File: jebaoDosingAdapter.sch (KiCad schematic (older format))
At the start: 4 parts, among them J1 Conn_01x05_Male, J2 Conn_01x02_Male, J3 6P6C, U1 ULN2803A

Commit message: Add images and updated gerbers
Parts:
- added H1, H2, H3, H4: MountingHole, MountingHole:MountingHole_3.2mm_M3, symbol Mechanical:MountingHole
- J1: footprint Connector_PinHeader_2.54mm:PinHeader_1x05_P2.54mm_Vertical -> Connector_JST:JST_XH_B05B-XH-A_1x05_P2.50mm_Vertical
- J2: footprint Connector_PinHeader_2.54mm:PinHeader_1x02_P2.54mm_Vertical -> Connector_JST:JST_XH_B02B-XH-A_1x02_P2.50mm_Vertical
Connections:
- net O1: now reaches J3.4
- net O1: now also U1.18 (O1); no longer U1.15 (O4)
- net O2: now reaches J3.2
- net O2: now also U1.17 (O2); no longer U1.16 (O3)
- net O3: now reaches J3.3
- net O3: now also U1.16 (O3); no longer U1.17 (O2)
- net O4: now reaches J3.5
- net O4: now also U1.15 (O4); no longer U1.18 (O1)
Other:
- moved on the sheet: J3
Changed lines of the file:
@@
 EESchema Schematic File Version 4
 LIBS:jebaoDosingAdapter-cache
-EELAYER 29 0
+EELAYER 26 0
 EELAYER END
 $Descr A4 11693 8268
@@
 $EndComp
 $Comp
-L Connector:6P6C J3
-U 1 1 5D71C0A6
-P 6600 2750
-F 0 "J3" H 6270 2754 50  0000 R CNN
-F 1 "6P6C" H 6270 2845 50  0000 R CNN
-F 2 "jebaoDosingAdapter:RJ11" V 6600 2775 50  0001 C CNN
-F 3 "~" V 6600 2775 50  0001 C CNN
-	1    6600 2750
-	-1   0    0    -1
-$EndComp
-$Comp
 L Connector:Conn_01x02_Male J2
 U 1 1 5D71C249
@@
 F 0 "J2" H 6706 3628 50  0000 C CNN
 F 1 "Conn_01x02_Male" H 6300 3400 50  0000 C CNN
-F 2 "Connector_PinHeader_2.54mm:PinHeader_1x02_P2.54mm_Vertical" H 6600 3450 50  0001 C CNN
+F 2 "Connector_JST:JST_XH_B02B-XH-A_1x02_P2.50mm_Vertical" H 6600 3450 50  0001 C CNN
 F 3 "~" H 6600 3450 50  0001 C CNN
 	1    6600 3450
@@
 F 0 "J1" H 4356 3128 50  0000 C CNN
 F 1 "Conn_01x05_Male" H 4356 3037 50  0000 C CNN
-F 2 "Connector_PinHeader_2.54mm:PinHeader_1x05_P2.54mm_Vertical" H 4250 2750 50  0001 C CNN
+F 2 "Connector_JST:JST_XH_B05B-XH-A_1x05_P2.50mm_Vertical" H 4250 2750 50  0001 C CNN
 F 3 "~" H 4250 2750 50  0001 C CNN
 	1    4250 2750
@@
 L power:+12V #PWR04
 U 1 1 5D71CEE9
-P 6150 3000
-F 0 "#PWR04" H 6150 2850 50  0001 C CNN
-F 1 "+12V" H 6165 3173 50  0000 C CNN
-F 2 "" H 6150 3000 50  0001 C CNN
-F 3 "" H 6150 3000 50  0001 C CNN
-	1    6150 3000
+P 6700 2850
+F 0 "#PWR04" H 6700 2700 50  0001 C CNN
+F 1 "+12V" H 6715 3023 50  0000 C CNN
+F 2 "" H 6700 2850 50  0001 C CNN
+F 3 "" H 6700 2850 50  0001 C CNN
+	1    6700 2850
 	1    0    0    1
 $EndComp
 Wire Wire Line
-	6150 3000 6150 2950
-Wire Wire Line
-	6150 2950 6200 2950
+	6700 2850 6700 2800
+Wire Wire Line
+	6700 2800 6750 2800
 $Comp
 L power:+12V #PWR05
 U 1 1 5D7302C7
-P 6150 2450
-F 0 "#PWR05" H 6150 2300 50  0001 C CNN
-F 1 "+12V" V 6165 2578 50  0000 L CNN
-F 2 "" H 6150 2450 50  0001 C CNN
-F 3 "" H 6150 2450 50  0001 C CNN
-	1    6150 2450
-	0    -1   1    0
-$EndComp
-Wire Wire Line
-	6200 2450 6150 2450
-Wire Wire Line
-	6200 2550 5700 2550
-Wire Wire Line
-	6200 2750 5950 2750
-Wire Wire Line
-	5950 2750 5950 2650
-Wire Wire Line
-	5950 2650 5700 2650
-Wire Wire Line
-	6200 2850 5900 2850
-Wire Wire Line
-	5900 2850 5900 2750
-Wire Wire Line
-	5900 2750 5700 2750
-Wire Wire Line
-	6200 2650 6050 2650
-Wire Wire Line
-	6050 2650 6050 2900
-Wire Wire Line
-	6050 2900 5850 2900
-Wire Wire Line
-	5850 2900 5850 2850
-Wire Wire Line
-	5850 2850 5700 2850
+P 6700 2300
+F 0 "#PWR05" H 6700 2150 50  0001 C CNN
+F 1 "+12V" H 6600 2450 50  0000 L CNN
+F 2 "" H 6700 2300 50  0001 C CNN
+F 3 "" H 6700 2300 50  0001 C CNN
+	1    6700 2300
+	-1   0    0    -1
+$EndComp
+Wire Wire Line
+	6750 2300 6700 2300
+$Comp
+L Mechanical:MountingHole H1
+U 1 1 5D9A0E71
+P 7850 2550
+F 0 "H1" H 7950 2596 50  0000 L CNN
+F 1 "MountingHole" H 7950 2505 50  0000 L CNN
+F 2 "MountingHole:MountingHole_3.2mm_M3" H 7850 2550 50  0001 C CNN
+F 3 "~" H 7850 2550 50  0001 C CNN
+	1    7850 2550
+	1    0    0    -1
+$EndComp
+$Comp
+L Mechanical:MountingHole H2
+U 1 1 5D9A0EAC
+P 7850 2750
+F 0 "H2" H 7950 2796 50  0000 L CNN
+F 1 "MountingHole" H 7950 2705 50  0000 L CNN
+F 2 "MountingHole:MountingHole_3.2mm_M3" H 7850 2750 50  0001 C CNN
+F 3 "~" H 7850 2750 50  0001 C CNN
+	1    7850 2750
+	1    0    0    -1
+$EndComp
+$Comp
+L Mechanical:MountingHole H3
+U 1 1 5D9A0ED0
+P 7850 2950
+F 0 "H3" H 7950 2996 50  0000 L CNN
+F 1 "MountingHole" H 7950 2905 50  0000 L CNN
+F 2 "MountingHole:MountingHole_3.2mm_M3" H 7850 2950 50  0001 C CNN
+F 3 "~" H 7850 2950 50  0001 C CNN
+	1    7850 2950
+	1    0    0    -1
+$EndComp
+$Comp
+L Mechanical:MountingHole H4
+U 1 1 5D9A0EFA
+P 7850 3150
+F 0 "H4" H 7950 3196 50  0000 L CNN
+F 1 "MountingHole" H 7950 3105 50  0000 L CNN
+F 2 "MountingHole:MountingHole_3.2mm_M3" H 7850 3150 50  0001 C CNN
+F 3 "~" H 7850 3150 50  0001 C CNN
+	1    7850 3150
+	1    0    0    -1
+$EndComp
+$Comp
+L Connector:6P6C J3
+U 1 1 5D71C0A6
+P 7150 2600
+F 0 "J3" H 6820 2604 50  0000 R CNN
+F 1 "6P6C" H 6820 2695 50  0000 R CNN
+F 2 "jebaoDosingAdapter:RJ11" V 7150 2625 50  0001 C CNN
+F 3 "~" V 7150 2625 50  0001 C CNN
+	1    7150 2600
+	-1   0    0    -1
+$EndComp
+Wire Wire Line
+	5700 2550 5900 2550
+Wire Wire Line
+	5700 2650 5900 2650
+Wire Wire Line
+	5700 2750 5900 2750
+Wire Wire Line
+	5700 2850 5900 2850
+Wire Wire Line
+	6750 2400 6450 2400
+Wire Wire Line
+	6750 2500 6450 2500
+Wire Wire Line
+	6750 2600 6450 2600
+Wire Wire Line
+	6750 2700 6450 2700
+Text Label 5900 2550 0    50   ~ 0
+O1
+Text Label 6450 2500 0    50   ~ 0
+O1
+Text Label 5900 2650 0    50   ~ 0
+O2
+Text Label 6450 2700 0    50   ~ 0
+O2
+Text Label 5900 2750 0    50   ~ 0
+O3
+Text Label 6450 2600 0    50   ~ 0
+O3
+Text Label 5900 2850 0    50   ~ 0
+O4
+Text Label 6450 2400 0    50   ~ 0
+O4
 $EndSCHEMATC

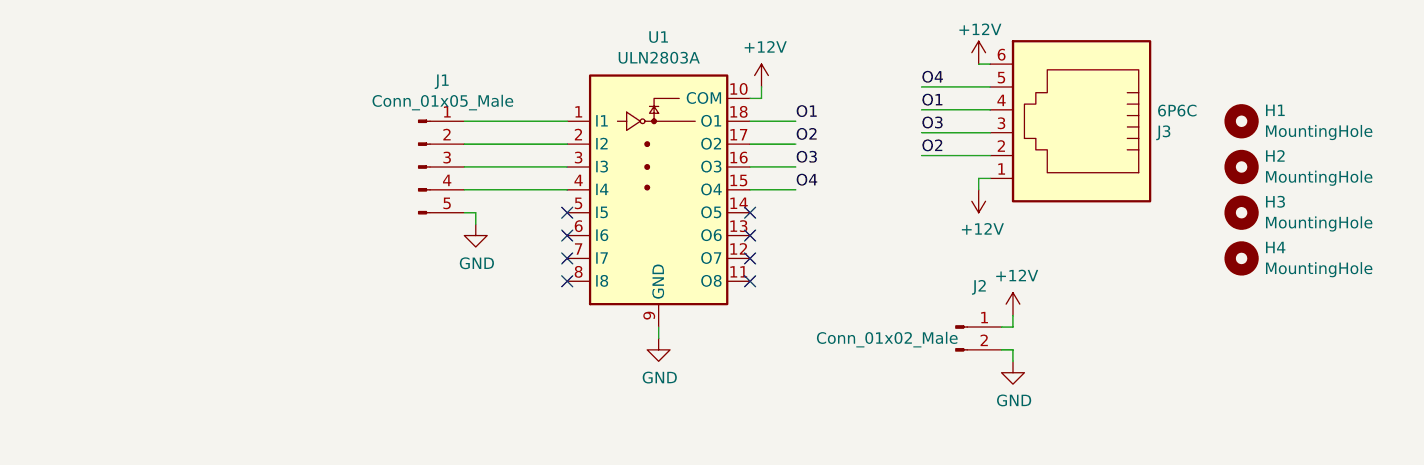
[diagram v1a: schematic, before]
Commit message: Double up driver and document
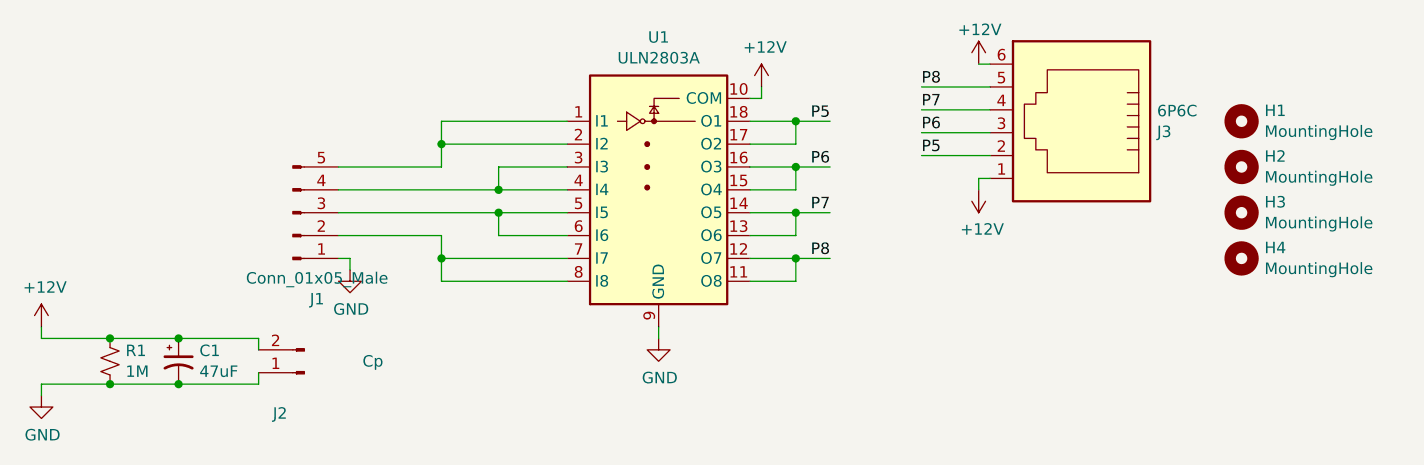
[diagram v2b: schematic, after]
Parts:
- added C1: 47uF, Capacitor_THT:CP_Radial_D6.3mm_P2.50mm, symbol Device:CP1_Small
- added R1: 1M, Resistors:0603, symbol Device:R_Small_US
- J2: value Conn_01x02_Male -> Cp
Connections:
- net O2 is gone; now on net P5: J3.2, U1.17 (O2)
- net +12V: now also J2.2 (Pin_2), C1.1, R1.1; no longer J2.1 (Pin_1)
- net GND: now also J1.1 (Pin_1), J2.1 (Pin_1), C1.2, R1.2; no longer J1.5 (Pin_5), J2.2 (Pin_2)
- net at U1.1 (I1): now also J1.5 (Pin_5), U1.2 (I2); no longer J1.1 (Pin_1)
- net P8: now reaches U1.11 (O8)
- net P8: now also J3.5, U1.12 (O7)
- net P7: now reaches U1.13 (O6)
- net P7: now also J3.4, U1.14 (O5)
- net at J1.2 (Pin_2): now also U1.7 (I7), U1.8 (I8); no longer U1.2 (I2)
- net at U1.3 (I3): now also J1.4 (Pin_4), U1.4 (I4); no longer J1.3 (Pin_3)
- net at U1.5 (I5): now also J1.3 (Pin_3), U1.6 (I6)
- net O1 renamed P5
- net P5: no longer J3.4
- net O3 renamed P6
- net P6: now also U1.15 (O4)
- removed net O4: J3.5, U1.15 (O4)
- no-connect marks 8 -> 0
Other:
- moved on the sheet: J1, J2
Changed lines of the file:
@@
 L Connector:Conn_01x02_Male J2
 U 1 1 5D71C249
-P 6600 3450
-F 0 "J2" H 6706 3628 50  0000 C CNN
-F 1 "Conn_01x02_Male" H 6300 3400 50  0000 C CNN
-F 2 "Connector_JST:JST_XH_B02B-XH-A_1x02_P2.50mm_Vertical" H 6600 3450 50  0001 C CNN
-F 3 "~" H 6600 3450 50  0001 C CNN
-	1    6600 3450
-	1    0    0    -1
+P 3750 3650
+F 0 "J2" H 3856 3828 50  0000 C CNN
+F 1 "Cp" H 3450 3600 50  0000 C CNN
+F 2 "Connector_JST:JST_XH_B02B-XH-A_1x02_P2.50mm_Vertical" H 3750 3650 50  0001 C CNN
+F 3 "~" H 3750 3650 50  0001 C CNN
+	1    3750 3650
+	-1   0    0    1
 $EndComp
 $Comp
 L power:GND #PWR07
 U 1 1 5D71C2D3
-P 6850 3600
-F 0 "#PWR07" H 6850 3350 50  0001 C CNN
-F 1 "GND" H 6855 3427 50  0000 C CNN
-F 2 "" H 6850 3600 50  0001 C CNN
-F 3 "" H 6850 3600 50  0001 C CNN
-	1    6850 3600
+P 2600 3750
+F 0 "#PWR07" H 2600 3500 50  0001 C CNN
+F 1 "GND" H 2605 3577 50  0000 C CNN
+F 2 "" H 2600 3750 50  0001 C CNN
+F 3 "" H 2600 3750 50  0001 C CNN
+	1    2600 3750
 	1    0    0    -1
 $EndComp
@@
 	5300 3450 5300 3500
 Wire Wire Line
-	6800 3550 6850 3550
-Wire Wire Line
-	6850 3550 6850 3600
+	2600 3700 2600 3750
 $Comp
 L power:GND #PWR01
 U 1 1 5D71C336
-P 4500 3000
-F 0 "#PWR01" H 4500 2750 50  0001 C CNN
-F 1 "GND" H 4505 2827 50  0000 C CNN
-F 2 "" H 4500 3000 50  0001 C CNN
-F 3 "" H 4500 3000 50  0001 C CNN
-	1    4500 3000
+P 3950 3200
+F 0 "#PWR01" H 3950 2950 50  0001 C CNN
+F 1 "GND" H 3955 3027 50  0000 C CNN
+F 2 "" H 3950 3200 50  0001 C CNN
+F 3 "" H 3950 3200 50  0001 C CNN
+	1    3950 3200
 	1    0    0    -1
 $EndComp
@@
 L power:+12V #PWR06
 U 1 1 5D71C3DD
-P 6850 3400
-F 0 "#PWR06" H 6850 3250 50  0001 C CNN
-F 1 "+12V" H 6865 3573 50  0000 C CNN
-F 2 "" H 6850 3400 50  0001 C CNN
-F 3 "" H 6850 3400 50  0001 C CNN
-	1    6850 3400
+P 2600 3450
+F 0 "#PWR06" H 2600 3300 50  0001 C CNN
+F 1 "+12V" H 2615 3623 50  0000 C CNN
+F 2 "" H 2600 3450 50  0001 C CNN
+F 3 "" H 2600 3450 50  0001 C CNN
+	1    2600 3450
 	1    0    0    -1
 $EndComp
@@
 L Connector:Conn_01x05_Male J1
 U 1 1 5D71C4F3
-P 4250 2750
-F 0 "J1" H 4356 3128 50  0000 C CNN
-F 1 "Conn_01x05_Male" H 4356 3037 50  0000 C CNN
-F 2 "Connector_JST:JST_XH_B05B-XH-A_1x05_P2.50mm_Vertical" H 4250 2750 50  0001 C CNN
-F 3 "~" H 4250 2750 50  0001 C CNN
-	1    4250 2750
-	1    0    0    -1
-$EndComp
-Wire Wire Line
-	4450 2950 4500 2950
-Wire Wire Line
-	4500 2950 4500 3000
-Wire Wire Line
-	4900 2550 4450 2550
-Wire Wire Line
-	4450 2650 4900 2650
-Wire Wire Line
-	4900 2750 4450 2750
-Wire Wire Line
-	4450 2850 4900 2850
-NoConn ~ 4900 2950
-NoConn ~ 4900 3050
-NoConn ~ 4900 3150
-NoConn ~ 4900 3250
-NoConn ~ 5700 3250
-NoConn ~ 5700 3150
-NoConn ~ 5700 3050
-NoConn ~ 5700 2950
-Wire Wire Line
-	6850 3400 6850 3450
-Wire Wire Line
-	6850 3450 6800 3450
+P 3700 2950
+F 0 "J1" H 3806 3328 50  0000 C CNN
+F 1 "Conn_01x05_Male" H 3806 3237 50  0000 C CNN
+F 2 "Connector_JST:JST_XH_B05B-XH-A_1x05_P2.50mm_Vertical" H 3700 2950 50  0001 C CNN
+F 3 "~" H 3700 2950 50  0001 C CNN
+	1    3700 2950
+	1    0    0    1
+$EndComp
+Wire Wire Line
+	3900 3150 3950 3150
+Wire Wire Line
+	3950 3150 3950 3200
+Wire Wire Line
+	4350 2750 3900 2750
+Wire Wire Line
+	3900 3050 4350 3050
+Wire Wire Line
+	2600 3450 2600 3500
 $Comp
 L power:+12V #PWR04
@@
 $EndComp
 Wire Wire Line
+	5700 2650 5900 2650
+Wire Wire Line
+	5700 2850 5900 2850
+Wire Wire Line
+	6750 2400 6450 2400
+Wire Wire Line
+	6750 2500 6450 2500
+Wire Wire Line
+	6750 2600 6450 2600
+Wire Wire Line
+	6750 2700 6450 2700
+Text Label 6050 2950 2    50   ~ 0
+P7
+Text Label 6450 2500 0    50   ~ 0
+P7
+Text Label 6050 2550 2    50   ~ 0
+P5
+Text Label 6450 2700 0    50   ~ 0
+P5
+Text Label 6050 2750 2    50   ~ 0
+P6
+Text Label 6450 2600 0    50   ~ 0
+P6
+Text Label 6050 3150 2    50   ~ 0
+P8
+Text Label 6450 2400 0    50   ~ 0
+P8
+Wire Wire Line
+	4350 2750 4350 2650
+Wire Wire Line
+	4350 2550 4900 2550
+Wire Wire Line
+	4900 2750 4600 2750
+Wire Wire Line
+	4600 2750 4600 2850
+Wire Wire Line
+	3900 2850 4600 2850
+Wire Wire Line
+	4900 3150 4350 3150
+Wire Wire Line
+	4350 3150 4350 3050
+Wire Wire Line
+	3900 2950 4600 2950
+Wire Wire Line
+	4350 3150 4350 3250
+Wire Wire Line
+	4350 3250 4900 3250
+Connection ~ 4350 3150
+Wire Wire Line
+	4900 3050 4600 3050
+Wire Wire Line
+	4600 3050 4600 2950
+Connection ~ 4600 2950
+Wire Wire Line
+	4600 2950 4900 2950
+Wire Wire Line
+	4900 2850 4600 2850
+Connection ~ 4600 2850
+Wire Wire Line
+	4900 2650 4350 2650
+Connection ~ 4350 2650
+Wire Wire Line
+	4350 2650 4350 2550
+Wire Wire Line
 	5700 2550 5900 2550
 Wire Wire Line
-	5700 2650 5900 2650
+	5900 2650 5900 2550
+Connection ~ 5900 2550
+Wire Wire Line
+	5900 2550 6050 2550
 Wire Wire Line
 	5700 2750 5900 2750
 Wire Wire Line
-	5700 2850 5900 2850
-Wire Wire Line
-	6750 2400 6450 2400
-Wire Wire Line
-	6750 2500 6450 2500
-Wire Wire Line
-	6750 2600 6450 2600
-Wire Wire Line
-	6750 2700 6450 2700
-Text Label 5900 2550 0    50   ~ 0
-O1
-Text Label 6450 2500 0    50   ~ 0
-O1
-Text Label 5900 2650 0    50   ~ 0
-O2
-Text Label 6450 2700 0    50   ~ 0
-O2
-Text Label 5900 2750 0    50   ~ 0
-O3
-Text Label 6450 2600 0    50   ~ 0
-O3
-Text Label 5900 2850 0    50   ~ 0
-O4
-Text Label 6450 2400 0    50   ~ 0
-O4
+	5900 2850 5900 2750
+Connection ~ 5900 2750
+Wire Wire Line
+	5900 2750 6050 2750
+Wire Wire Line
+	5700 2950 5900 2950
+Wire Wire Line
+	5900 2950 5900 3050
+Wire Wire Line
+	5900 3050 5700 3050
+Connection ~ 5900 2950
+Wire Wire Line
+	5900 2950 6050 2950
+Wire Wire Line
+	5700 3150 5900 3150
+Wire Wire Line
+	5700 3250 5900 3250
+Wire Wire Line
+	5900 3250 5900 3150
+Connection ~ 5900 3150
+Wire Wire Line
+	5900 3150 6050 3150
+$Comp
+L Device:CP1_Small C1
+U 1 1 5E5B154D
+P 3200 3600
+F 0 "C1" H 3291 3646 50  0000 L CNN
+F 1 "47uF" H 3291 3555 50  0000 L CNN
+F 2 "Capacitor_THT:CP_Radial_D6.3mm_P2.50mm" H 3200 3600 50  0001 C CNN
+F 3 "~" H 3200 3600 50  0001 C CNN
+	1    3200 3600
+	1    0    0    -1
+$EndComp
+$Comp
+L Device:R_Small_US R1
+U 1 1 5E5B1649
+P 2900 3600
+F 0 "R1" H 2968 3646 50  0000 L CNN
+F 1 "1M" H 2968 3555 50  0000 L CNN
+F 2 "Resistors:0603" H 2900 3600 50  0001 C CNN
+F 3 "~" H 2900 3600 50  0001 C CNN
+	1    2900 3600
+	1    0    0    -1
+$EndComp
+Wire Wire Line
+	2600 3500 2900 3500
+Wire Wire Line
+	2600 3700 2900 3700
+Wire Wire Line
+	3200 3500 2900 3500
+Connection ~ 2900 3500
+Wire Wire Line
+	3200 3700 2900 3700
+Connection ~ 2900 3700
+Wire Wire Line
+	3550 3550 3550 3500
+Wire Wire Line
+	3550 3500 3200 3500
+Connection ~ 3200 3500
+Wire Wire Line
+	3550 3650 3550 3700
+Wire Wire Line
+	3550 3700 3200 3700
+Connection ~ 3200 3700
 $EndSCHEMATC
